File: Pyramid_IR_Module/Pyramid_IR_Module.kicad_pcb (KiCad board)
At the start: 2 copper layers, 20.3 x 9.5 mm, 8 parts, among them P1 CONN_4, Q1 NPN

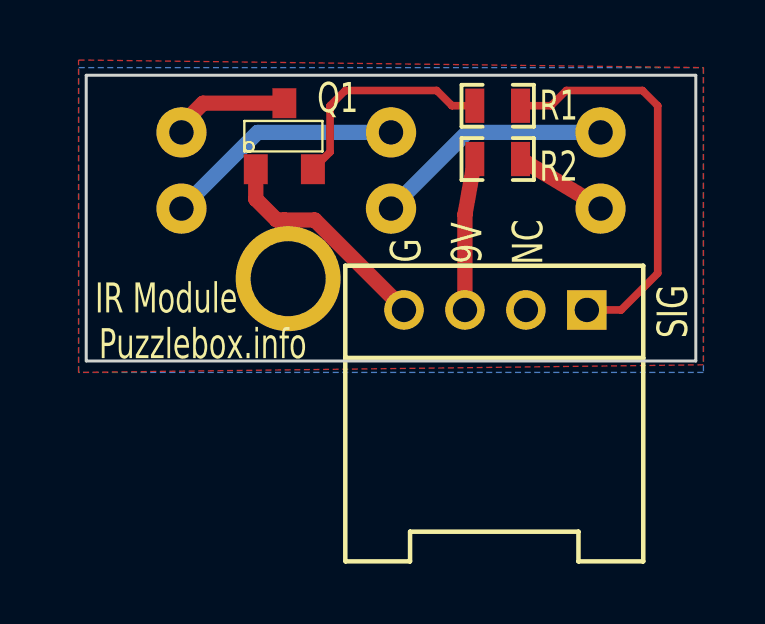
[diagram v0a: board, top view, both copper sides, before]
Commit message: fixed bugs on NPN and PNP library, IR module and Pyramid Shield
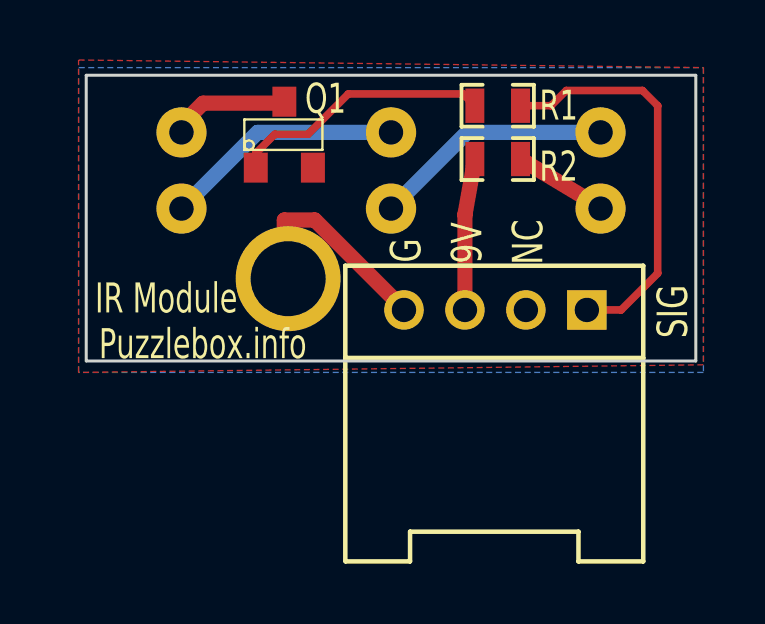
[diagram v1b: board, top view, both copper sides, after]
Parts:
- moved Q1 0.05 mm to (225.0, 155.9)
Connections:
- Q1 pad 1: GND -> N-000009
- Q1 pad 2: N-000009 -> GND
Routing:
- net GND: track 9.77 -> 7.53 mm
- net N-000009: track 7.60 -> 8.76 mm
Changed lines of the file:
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@@
     (links 9)
     (no_connects 0)
-    (area 218.019023 151.08555 239.97 170.458201)
+    (area 217.855035 143.665724 255.312915 170.458201)
     (thickness 1.6)
     (drawings 10)
-    (tracks 31)
+    (tracks 28)
     (zones 0)
     (modules 8)
@@
   (layers
     (15 F.Cu signal)
-    (0 B.Cu signal)
+    (0 B.Cu signal hide)
     (16 B.Adhes user)
     (17 F.Adhes user)
@@
     (visible_elements 7FFFFFFF)
     (pcbplotparams
-      (layerselection 272400385)
+      (layerselection 284983297)
       (usegerberextensions true)
       (excludeedgelayer true)
@@
   )
   (module LED-5MM (layer B.Cu)
-    (at 235.585 157.099 90)
+    (at 228.6 157.099 90)
     (descr "LED 5mm - Lead pitch 100mil (2,54mm)")
     (tags "LED led 5mm 5MM 100mil 2,54mm")
-    (fp_text reference D1 (at 2.3368 -3.4798 180) (layer B.SilkS)
+    (fp_text reference D2 (at 2.3368 -3.4798 180) (layer B.SilkS)
       (effects (font (size 1 0.7) (thickness 0.15)) (justify mirror))
     )
-    (fp_text value LED (at 4.445 -3.429 90) (layer B.SilkS) hide
+    (fp_text value LED (at 4.445 -3.556 90) (layer B.SilkS) hide
       (effects (font (size 0.762 0.762) (thickness 0.0889)) (justify mirror))
     )
@@
     (pad 1 thru_hole circle (at -1.27 0 90) (size 1.6764 1.6764) (drill 0.8128)
       (layers *.Cu *.Mask B.SilkS)
-      (net 2 /LED1)
+      (net 3 /LED2)
     )
     (pad 2 thru_hole circle (at 1.27 0 90) (size 1.6764 1.6764) (drill 0.8128)
       (layers *.Cu *.Mask B.SilkS)
-      (net 3 /LED2)
+      (net 4 /LED3)
     )
     (model discret/leds/led5_vertical_verde.wrl
@@
   )
   (module LED-5MM (layer B.Cu)
-    (at 228.6 157.099 90)
+    (at 235.585 157.099 90)
     (descr "LED 5mm - Lead pitch 100mil (2,54mm)")
     (tags "LED led 5mm 5MM 100mil 2,54mm")
-    (fp_text reference D2 (at 2.3368 -3.4798 180) (layer B.SilkS)
+    (fp_text reference D1 (at 2.3368 -3.4798 180) (layer B.SilkS)
       (effects (font (size 1 0.7) (thickness 0.15)) (justify mirror))
     )
-    (fp_text value LED (at 4.445 -3.556 90) (layer B.SilkS) hide
+    (fp_text value LED (at 4.445 -3.429 90) (layer B.SilkS) hide
       (effects (font (size 0.762 0.762) (thickness 0.0889)) (justify mirror))
     )
@@
     (pad 1 thru_hole circle (at -1.27 0 90) (size 1.6764 1.6764) (drill 0.8128)
       (layers *.Cu *.Mask B.SilkS)
+      (net 2 /LED1)
+    )
+    (pad 2 thru_hole circle (at 1.27 0 90) (size 1.6764 1.6764) (drill 0.8128)
+      (layers *.Cu *.Mask B.SilkS)
       (net 3 /LED2)
-    )
-    (pad 2 thru_hole circle (at 1.27 0 90) (size 1.6764 1.6764) (drill 0.8128)
-      (layers *.Cu *.Mask B.SilkS)
-      (net 4 /LED3)
     )
     (model discret/leds/led5_vertical_verde.wrl
@@
       (scale (xyz 1 1 1))
       (rotate (xyz 0 0 0))
-    )
-  )
-  (module SOT23 (layer F.Cu)
-    (at 225.044 155.956)
-    (tags SOT23)
-    (fp_text reference Q1 (at 1.778 -1.27) (layer F.SilkS)
-      (effects (font (size 1 0.7) (thickness 0.15)))
-    )
-    (fp_text value NPN (at 3.556 -1.27) (layer F.SilkS) hide
-      (effects (font (size 1 0.7) (thickness 0.15)))
-    )
-    (fp_circle (center -1.17602 0.35052) (end -1.30048 0.44958) (layer F.SilkS) (width 0.07874))
-    (fp_line (start 1.27 -0.508) (end 1.27 0.508) (layer F.SilkS) (width 0.07874))
-    (fp_line (start -1.3335 -0.508) (end -1.3335 0.508) (layer F.SilkS) (width 0.07874))
-    (fp_line (start 1.27 0.508) (end -1.3335 0.508) (layer F.SilkS) (width 0.07874))
-    (fp_line (start -1.3335 -0.508) (end 1.27 -0.508) (layer F.SilkS) (width 0.07874))
-    (pad 3 smd rect (at 0 -1.09982) (size 0.8001 1.00076)
-      (layers F.Cu F.Paste F.Mask)
-      (net 5 /LED4)
-    )
-    (pad 2 smd rect (at 0.9525 1.09982) (size 0.8001 1.00076)
-      (layers F.Cu F.Paste F.Mask)
-      (net 8 N-000009)
-    )
-    (pad 1 smd rect (at -0.9525 1.09982) (size 0.8001 1.00076)
-      (layers F.Cu F.Paste F.Mask)
-      (net 6 GND)
-    )
-    (model smd\SOT23_3.wrl
-      (at (xyz 0 0 0))
-      (scale (xyz 0.4 0.4 0.4))
-      (rotate (xyz 0 0 180))
     )
   )
@@
       (layers *.Cu *.Mask F.SilkS)
       (net 7 N-000004)
+    )
+  )
+  (module SOT23 (layer F.Cu)
+    (at 225.044 155.9052)
+    (tags SOT23)
+    (fp_text reference Q1 (at 1.3716 -1.1938) (layer F.SilkS)
+      (effects (font (size 1 0.7) (thickness 0.15)))
+    )
+    (fp_text value NPN (at 0.0254 0.1016) (layer F.SilkS) hide
+      (effects (font (size 1 0.7) (thickness 0.15)))
+    )
+    (fp_circle (center -1.17602 0.35052) (end -1.30048 0.44958) (layer F.SilkS) (width 0.07874))
+    (fp_line (start 1.27 -0.508) (end 1.27 0.508) (layer F.SilkS) (width 0.07874))
+    (fp_line (start -1.3335 -0.508) (end -1.3335 0.508) (layer F.SilkS) (width 0.07874))
+    (fp_line (start 1.27 0.508) (end -1.3335 0.508) (layer F.SilkS) (width 0.07874))
+    (fp_line (start -1.3335 -0.508) (end 1.27 -0.508) (layer F.SilkS) (width 0.07874))
+    (pad 3 smd rect (at 0 -1.09982) (size 0.8001 1.00076)
+      (layers F.Cu F.Paste F.Mask)
+      (net 5 /LED4)
+    )
+    (pad 2 smd rect (at 0.9525 1.09982) (size 0.8001 1.00076)
+      (layers F.Cu F.Paste F.Mask)
+      (net 6 GND)
+    )
+    (pad 1 smd rect (at -0.9525 1.09982) (size 0.8001 1.00076)
+      (layers F.Cu F.Paste F.Mask)
+      (net 8 N-000009)
+    )
+    (model smd\SOT23_3.wrl
+      (at (xyz 0 0 0))
+      (scale (xyz 0.4 0.4 0.4))
+      (rotate (xyz 0 0 180))
     )
   )
@@
   (segment (start 229.0318 161.7218) (end 226.06 158.75) (width 0.508) (layer F.Cu) (net 6))
   (segment (start 225.044 161.036) (end 225.044 158.75) (width 0.508) (layer F.Cu) (net 6))
-  (segment (start 224.0915 157.05582) (end 224.0915 158.0515) (width 0.508) (layer F.Cu) (net 6))
-  (segment (start 224.79 158.75) (end 225.044 158.75) (width 0.508) (layer F.Cu) (net 6))
-  (segment (start 224.0915 158.0515) (end 224.79 158.75) (width 0.508) (layer F.Cu) (net 6))
   (segment (start 232.918 154.94) (end 233.934 154.94) (width 0.254) (layer F.Cu) (net 7))
   (segment (start 236.2708 161.7472) (end 235.1278 161.7472) (width 0.254) (layer F.Cu) (net 7))
@@
   (segment (start 234.442 154.432) (end 236.982 154.432) (width 0.254) (layer F.Cu) (net 7))
   (segment (start 233.934 154.94) (end 234.442 154.432) (width 0.254) (layer F.Cu) (net 7))
-  (segment (start 231.394 154.94) (end 230.632 154.94) (width 0.254) (layer F.Cu) (net 8))
-  (segment (start 226.568 156.48432) (end 225.9965 157.05582) (width 0.254) (layer F.Cu) (net 8))
-  (segment (start 226.568 154.94) (end 226.568 156.48432) (width 0.254) (layer F.Cu) (net 8))
-  (segment (start 227.076 154.432) (end 226.568 154.94) (width 0.254) (layer F.Cu) (net 8))
-  (segment (start 230.124 154.432) (end 227.076 154.432) (width 0.254) (layer F.Cu) (net 8))
-  (segment (start 230.632 154.94) (end 230.124 154.432) (width 0.254) (layer F.Cu) (net 8))
+  (segment (start 224.0915 157.00502) (end 224.0915 156.5275) (width 0.254) (layer F.Cu) (net 8))
+  (segment (start 231.0003 154.5463) (end 231.394 154.94) (width 0.254) (layer F.Cu) (net 8))
+  (segment (start 227.1776 154.5463) (end 231.0003 154.5463) (width 0.254) (layer F.Cu) (net 8))
+  (segment (start 225.8314 155.8925) (end 227.1776 154.5463) (width 0.254) (layer F.Cu) (net 8))
+  (segment (start 224.7265 155.8925) (end 225.8314 155.8925) (width 0.254) (layer F.Cu) (net 8))
+  (segment (start 224.0915 156.5275) (end 224.7265 155.8925) (width 0.254) (layer F.Cu) (net 8))
   (zone (net 6) (net_name GND) (layer F.Cu) (hatch edge 0.508)
     (connect_pads (clearance 0.508))

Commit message: New Product Importing
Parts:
- R1: value 820 -> 820R
- R2: value 82 -> 82R
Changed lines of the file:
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@@
       (effects (font (size 1 0.7) (thickness 0.15)))
     )
-    (fp_text value 82 (at 3.556 0.254) (layer F.SilkS) hide
+    (fp_text value 82R (at 3.556 0.254) (layer F.SilkS) hide
       (effects (font (size 1 0.7) (thickness 0.15)))
     )
@@
       (effects (font (size 1 0.7) (thickness 0.15)))
     )
-    (fp_text value 820 (at -3.81 0 180) (layer F.SilkS) hide
+    (fp_text value 820R (at -3.81 0 180) (layer F.SilkS) hide
       (effects (font (size 1 0.7) (thickness 0.15)))
     )
@@
       (effects (font (size 1.016 0.762) (thickness 0.1524)))
     )
-    (fp_text user NC (at 0.7874 6.096 90) (layer F.SilkS)
+    (fp_text user NC (at 0.889 6.096 90) (layer F.SilkS)
       (effects (font (size 1.016 0.762) (thickness 0.1524)))
     )
